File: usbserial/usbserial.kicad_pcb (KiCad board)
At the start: 4 copper layers, 47.8 x 28.2 mm, 16 parts, among them J101 Conn_01x06, Q401 MMBT3904, Q402 MMBT3904, U401 USBLC6-2SC6, U402 CH340C

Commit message: add some labels
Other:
- board size 47.8 x 28.2 mm -> 55.2 x 28.2 mm
- board text added: "GND"
- board text added: "VUSB"
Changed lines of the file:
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@@
 		(tags "resistor")
 		(property "Reference" "R201"
-			(at 0 -1.43 360)
+			(at 0 -1.43 0)
 			(layer "F.SilkS")
 			(effects
@@
 		)
 		(property "Value" "5.1k"
-			(at 0 1.43 360)
+			(at 0 1.43 0)
 			(layer "F.Fab")
 			(effects
@@
 		)
 		(fp_text user "${REFERENCE}"
-			(at 0 0 360)
+			(at 0 0 0)
 			(layer "F.Fab")
 			(effects
@@
 		(tags "resistor")
 		(property "Reference" "R202"
-			(at 0 -1.43 360)
+			(at 0 -1.43 0)
 			(layer "F.SilkS")
 			(effects
@@
 		)
 		(property "Value" "5.1k"
-			(at 0 1.43 360)
+			(at 0 1.43 0)
 			(layer "F.Fab")
 			(effects
@@
 		)
 		(fp_text user "${REFERENCE}"
-			(at 0 0 360)
+			(at 0 0 0)
 			(layer "F.Fab")
 			(effects
@@
 	(gr_rect
 		(start 13.75 13)
-		(end 61.5 41.25)
+		(end 68.9 41.25)
 		(stroke
 			(width 0.05)
@@
 		(layer "Edge.Cuts")
 	)
+	(gr_text "VUSB"
+		(at 57.8 22 0)
+		(layer "F.SilkS")
+		(effects
+			(font
+				(size 1 1)
+				(thickness 0.1)
+			)
+			(justify left bottom)
+		)
+	)
+	(gr_text "GND"
+		(at 57.8 24.4 0)
+		(layer "F.SilkS")
+		(effects
+			(font
+				(size 1 1)
+				(thickness 0.1)
+			)
+			(justify left bottom)
+		)
+	)
 	(segment
 		(start 22.85 24.4)
@@
 		(polygon
 			(pts
-				(xy 14.25 13.5) (xy 61 13.5) (xy 61 40.75) (xy 14.25 40.5)
+				(xy 14.25 13.5) (xy 68.4 13.3) (xy 68.4 40.55) (xy 14.25 40.5)
 			)
 		)
@@
 		(polygon
 			(pts
-				(xy 14.25 13.5) (xy 61 13.5) (xy 61 40.75) (xy 14.25 40.5)
+				(xy 14.25 13.5) (xy 68.6 13.7) (xy 68.6 40.95) (xy 14.25 40.5)
 			)
 		)

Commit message: cleanup usb serial
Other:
- board size 55.2 x 28.2 mm -> 50.3 x 28.2 mm
- board text added: "BOOT"
- board text added: "RST"
- board text added: "RXD"
- board text added: "TXD"
- board text added: "USB-Serial v0.1"
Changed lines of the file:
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@@
 	(gr_rect
 		(start 13.75 13)
-		(end 68.9 41.25)
+		(end 64.1 41.25)
 		(stroke
 			(width 0.05)
@@
 		(fill none)
 		(layer "Edge.Cuts")
+	)
+	(gr_text "RXD"
+		(at 57.8 29.6 0)
+		(layer "F.SilkS")
+		(effects
+			(font
+				(size 1 1)
+				(thickness 0.1)
+			)
+			(justify left bottom)
+		)
 	)
 	(gr_text "VUSB"
@@
 		)
 	)
+	(gr_text "USB-Serial v0.1"
+		(at 17 16.8 0)
+		(layer "F.SilkS")
+		(effects
+			(font
+				(size 1 1)
+				(thickness 0.1)
+			)
+			(justify left bottom)
+		)
+	)
 	(gr_text "GND"
 		(at 57.8 24.4 0)
@@
 		)
 	)
+	(gr_text "TXD"
+		(at 57.8 27 0)
+		(layer "F.SilkS")
+		(effects
+			(font
+				(size 1 1)
+				(thickness 0.1)
+			)
+			(justify left bottom)
+		)
+	)
+	(gr_text "RST"
+		(at 57.8 34.8 0)
+		(layer "F.SilkS")
+		(effects
+			(font
+				(size 1 1)
+				(thickness 0.1)
+			)
+			(justify left bottom)
+		)
+	)
+	(gr_text "BOOT"
+		(at 57.8 32.2 0)
+		(layer "F.SilkS")
+		(effects
+			(font
+				(size 1 1)
+				(thickness 0.1)
+			)
+			(justify left bottom)
+		)
+	)
 	(segment
 		(start 22.85 24.4)
@@
 		(polygon
 			(pts
-				(xy 14.25 13.5) (xy 68.4 13.3) (xy 68.4 40.55) (xy 14.25 40.5)
+				(xy 14.25 13.5) (xy 63.2 13.7) (xy 63.2 40.95) (xy 14.25 40.5)
 			)
 		)
@@
 		(polygon
 			(pts
-				(xy 14.25 13.5) (xy 68.6 13.7) (xy 68.6 40.95) (xy 14.25 40.5)
+				(xy 14.25 13.5) (xy 63.2 13.7) (xy 63.2 40.95) (xy 14.25 40.5)
 			)
 		)

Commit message: usbserial 0.1 sent to fab
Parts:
- R402, R403: value 480 -> 487
- moved J101 5.46 mm to (61.2, 21.1)
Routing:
- net /usb_serial/RXD: track 14.5 -> 20.1 mm
- net /usb_serial/TXD: track 16.6 -> 22.1 mm
- net /usb_serial/BOOT: track 10.0 -> 15.4 mm
- net /usb_serial/RST: track 14.6 -> 19.9 mm
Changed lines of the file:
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@@
 			)
 		)
-		(property "Value" "480"
+		(property "Value" "487"
 			(at 0 1.43 0)
 			(layer "F.Fab")
@@
 			)
 		)
-		(property "Value" "480"
+		(property "Value" "487"
 			(at 0 1.43 0)
 			(layer "F.Fab")
@@
 	(footprint "Connector_PinHeader_2.54mm:PinHeader_1x06_P2.54mm_Vertical"
 		(layer "F.Cu")
-		(at 55.75 21.42)
+		(at 61.2 21.12)
 		(descr "Through hole straight pin header, 1x06, 2.54mm pitch, single row")
 		(tags "Through hole pin header THT 1x06 2.54mm single row")
@@
 	)
 	(gr_text "RXD"
-		(at 57.8 29.6 0)
+		(at 56 29.2 0)
 		(layer "F.SilkS")
 		(effects
@@
 	)
 	(gr_text "VUSB"
-		(at 57.8 22 0)
+		(at 56 21.6 0)
 		(layer "F.SilkS")
 		(effects
@@
 	)
 	(gr_text "GND"
-		(at 57.8 24.4 0)
+		(at 56 24 0)
 		(layer "F.SilkS")
 		(effects
@@
 	)
 	(gr_text "TXD"
-		(at 57.8 27 0)
+		(at 56 26.6 0)
 		(layer "F.SilkS")
 		(effects
@@
 	)
 	(gr_text "RST"
-		(at 57.8 34.8 0)
+		(at 56 34.4 0)
 		(layer "F.SilkS")
 		(effects
@@
 	)
 	(gr_text "BOOT"
-		(at 57.8 32.2 0)
+		(at 56 31.8 0)
 		(layer "F.SilkS")
 		(effects
@@
 	)
 	(segment
+		(start 55.45 33.82)
+		(end 61.2 33.82)
+		(width 0.2)
+		(layer "B.Cu")
+		(net 3)
+	)
+	(segment
 		(start 52.75 31.12)
-		(end 55.75 34.12)
+		(end 55.45 33.82)
 		(width 0.2)
 		(layer "B.Cu")
@@
 	)
 	(segment
-		(start 51.75 27.58)
-		(end 55.75 31.58)
+		(start 55.17 31)
+		(end 55.2 31)
+		(width 0.2)
+		(layer "B.Cu")
+		(net 7)
+	)
+	(segment
+		(start 55.48 31.28)
+		(end 61.2 31.28)
 		(width 0.2)
 		(layer "B.Cu")
@@
 	)
 	(segment
+		(start 55.2 31)
+		(end 55.48 31.28)
+		(width 0.2)
+		(layer "B.Cu")
+		(net 7)
+	)
+	(segment
+		(start 51.75 27.58)
+		(end 55.17 31)
+		(width 0.2)
+		(layer "B.Cu")
+		(net 7)
+	)
+	(segment
 		(start 40.025 29.25)
 		(end 43.4625 29.25)
@@
 	)
 	(segment
+		(start 56.05 26.2)
+		(end 61.2 26.2)
+		(width 0.2)
+		(layer "B.Cu")
+		(net 24)
+	)
+	(segment
 		(start 45.5 32.75)
 		(end 51.75 26.5)
@@
 	)
 	(segment
-		(start 42.025 31)
-		(end 53.79 31)
+		(start 55.75 26.5)
+		(end 56.05 26.2)
+		(width 0.2)
+		(layer "B.Cu")
+		(net 24)
+	)
+	(segment
+		(start 53.79 31)
+		(end 56.05 28.74)
 		(width 0.2)
 		(layer "F.Cu")
@@
 	)
 	(segment
-		(start 53.79 31)
-		(end 55.75 29.04)
+		(start 56.05 28.74)
+		(end 61.2 28.74)
+		(width 0.2)
+		(layer "F.Cu")
+		(net 25)
+	)
+	(segment
+		(start 42.025 31)
+		(end 53.79 31)
 		(width 0.2)
 		(layer "F.Cu")

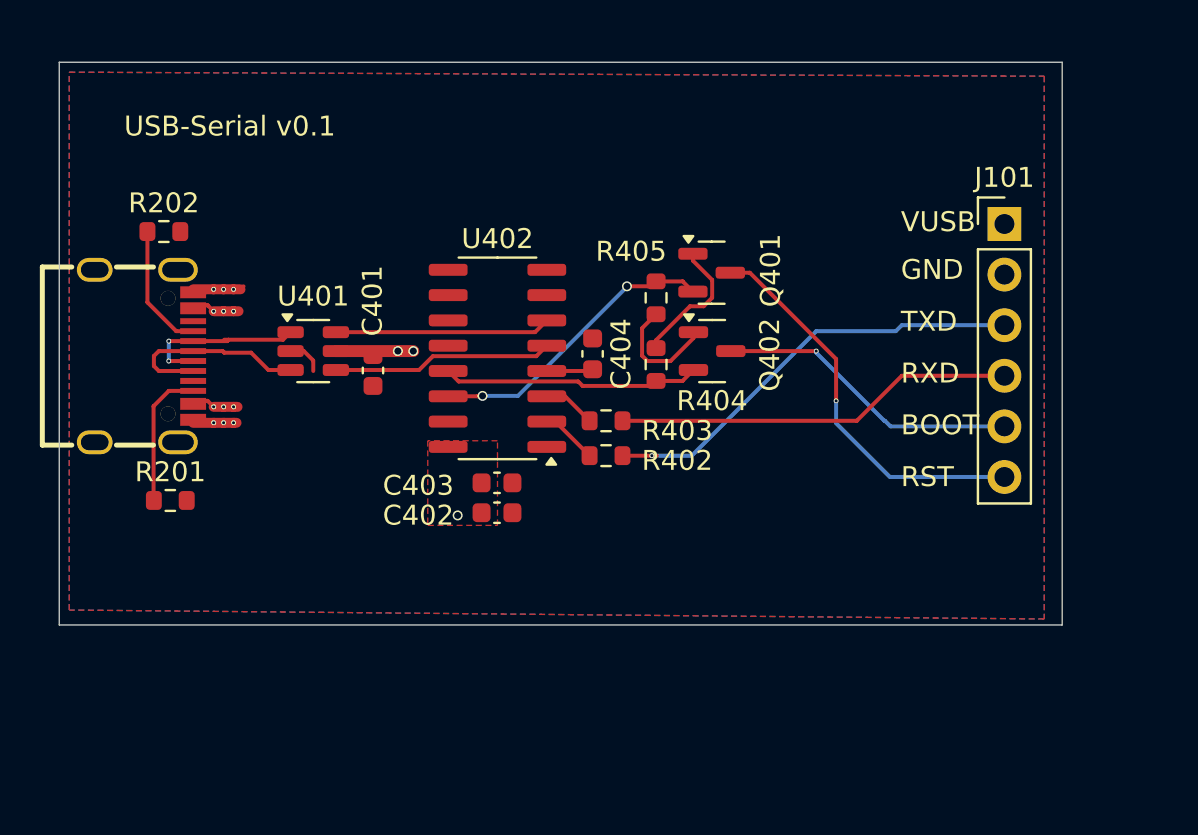
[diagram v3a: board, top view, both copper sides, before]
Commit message: fix via sizes
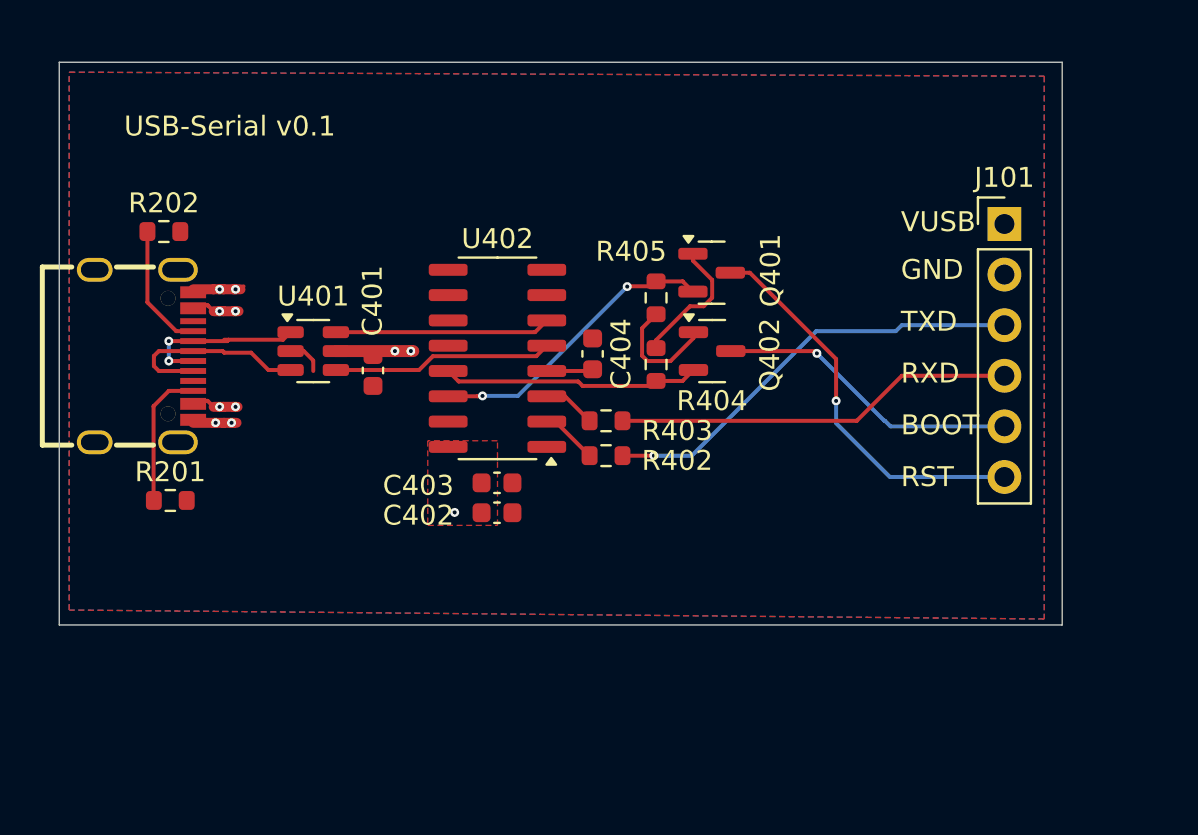
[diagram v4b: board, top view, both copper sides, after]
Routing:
- net GND: vias 6 -> 4
- net /usb_serial/VUSB: vias 9 -> 7

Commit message: work on usbserial
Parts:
- added C101: 1uF, Capacitor_SMD:C_0603_1608Metric, F.Cu at (52.8, 16.2)
- added C102: 1uF, Capacitor_SMD:C_0603_1608Metric, F.Cu at (52.8, 19.3)
- added C103: 1uF, Capacitor_SMD:C_0603_1608Metric, F.Cu at (51.2, 19.3)
- added C104: 10nF, Capacitor_SMD:C_0603_1608Metric, F.Cu at (52.0, 22.2)
- added J102: Conn_02x02_Counter_Clockwise, Connector_PinHeader_2.54mm:PinHeader_2x02_P2.54mm_Vertical, F.Cu at (51.2, 27.8)
- added R101: 10k, Resistor_SMD:R_0603_1608Metric, F.Cu at (46.8, 19.9)
- added U101: TPS73733DCQ_C5220270, easyeda2kicad:SOT-223-6_L6.5-W3.5-P1.27-LS7.0-BR, F.Cu at (58.0, 19.5)
- moved R202 23.5 mm to (42.2, 18.1), turned to -90 degrees
- moved Q401 22.9 mm to (40.2, 45.6), turned to -90 degrees
- moved USBC201 20.9 mm to (36.0, 17.1), turned to 180 degrees
- moved Q402 20.8 mm to (36.2, 45.6), turned to -90 degrees
- moved R201 19.1 mm to (28.8, 18.4), turned to -90 degrees
- moved R405 18.6 mm to (38.9, 42.8), turned to 0 degrees
- moved R404 16.7 mm to (35.6, 42.8), turned to 180 degrees
- moved C404 12.8 mm to (36.1, 39.6), turned to 180 degrees
- moved R402 12.7 mm to (31.0, 40.3), turned to -90 degrees
- moved R403 12.6 mm to (32.8, 40.3), turned to 90 degrees
- moved U401 9.93 mm to (36.2, 25.6), turned to -90 degrees
- moved C402 7.63 mm to (28.1, 34.8), turned to -90 degrees
- moved U402 6.99 mm to (35.9, 34.9), turned to 90 degrees
- moved C403 6.13 mm to (29.6, 34.8), turned to -90 degrees
- moved C401 5.78 mm to (35.3, 28.6), turned to 180 degrees
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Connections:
- J101 pad 1: /usb_serial/VUSB -> /PWR
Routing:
- net /usb_serial/RXD: track 20.1 -> 0.00 mm
- net /usb_serial/RST: track 19.9 -> 0.98 mm, vias 1 -> 0
- net /usb_serial/TXD: track 22.1 -> 3.73 mm
- net /usb_serial/BOOT: track 15.4 -> 0.00 mm, vias 1 -> 0
- net Net-(U101-NR/FB): track 0.00 -> 3.35 mm
- net GND: vias 4 -> 7
- added copper zone on F.Cu, net /3v3
- added copper zone on F.Cu, net /PWR
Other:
- board size 50.3 x 28.2 mm -> 40 x 36.8 mm
- board text added: "3v3"
- board text added: "PWR"

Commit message: usbserial v2
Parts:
- moved R101 11.5 mm to (57.0, 14.8), turned to 0 degrees
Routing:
- net /usb_serial/TXD: track 3.73 -> 41.1 mm
- net /usb_serial/RXD: track 0.00 -> 34.8 mm, vias 0 -> 1
- net /usb_serial/BOOT: track 0.00 -> 34.5 mm
- net /usb_serial/RST: track 0.98 -> 25.2 mm
- net Net-(U101-EN): track 0.00 -> 21.1 mm
- net GND: track 7.07 -> 9.70 mm, vias 7 -> 13
- net /usb_serial/VUSB: track 8.65 -> 10.9 mm, vias 7 -> 10
